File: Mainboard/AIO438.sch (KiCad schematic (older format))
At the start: 0 parts

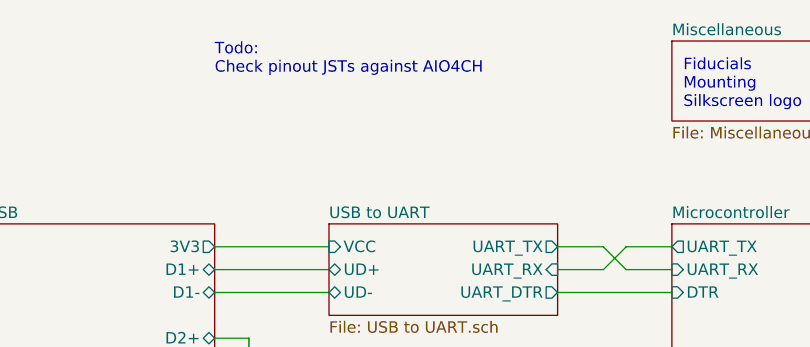
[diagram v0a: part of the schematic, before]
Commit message: Modify library references
As described in the README of the newly added libraries submodule.
Schematic and PCB are synced.

Hardware folder is renamed to mainboard
Any other PCBs can be put in their own subfolder in the gitrepo

Commit also swaps source/drain of Q1 because it appeared wrong for some
reason after updating all symbol/footprints.
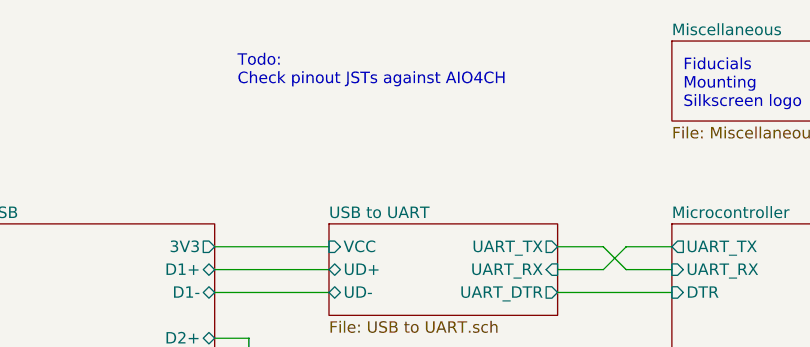
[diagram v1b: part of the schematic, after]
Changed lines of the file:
@@
 Wire Wire Line
 	6650 4200 6400 4200
-Text Notes 3350 1900 0    50   ~ 0
+Text Notes 3450 1950 0    50   ~ 0
 Todo:\nCheck pinout JSTs against AIO4CH
 Wire Wire Line

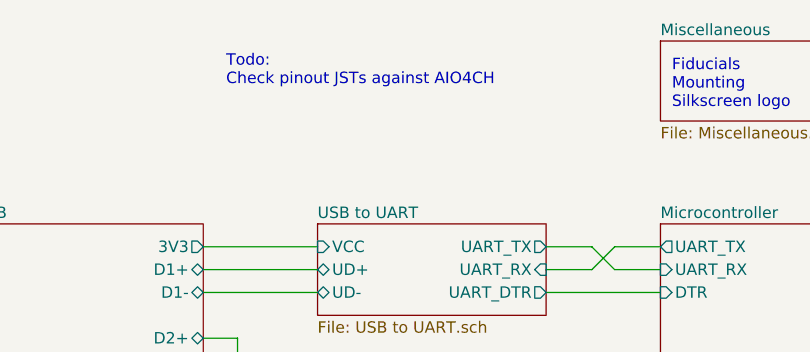
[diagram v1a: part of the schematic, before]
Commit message: Before power tree change
Backup before switching from two to one LDO
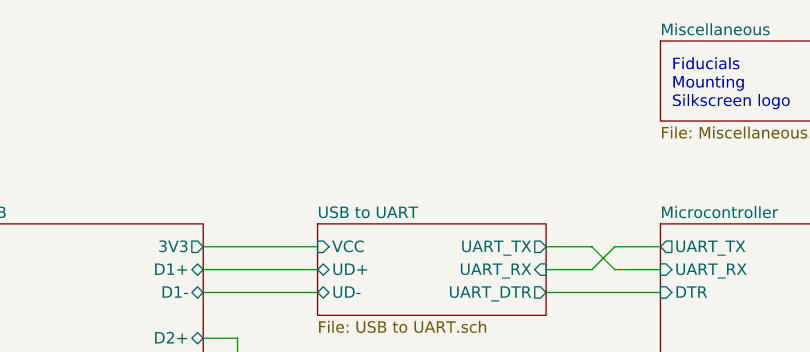
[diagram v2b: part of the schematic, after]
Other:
- note removed: "Todo:\nCheck pinout JSTs against AIO4CH"
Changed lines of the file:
@@
 Sheet 1 9
 Title "4x38W amp with DSP and BT"
-Date "2021-06-08"
-Rev "0.1"
+Date "2021-11-08"
+Rev "0.2"
 Comp "ZOUDIO"
 Comment1 ""
@@
 Wire Wire Line
 	6650 4200 6400 4200
-Text Notes 3450 1950 0    50   ~ 0
-Todo:\nCheck pinout JSTs against AIO4CH
 Wire Wire Line
 	3350 3150 3450 3150

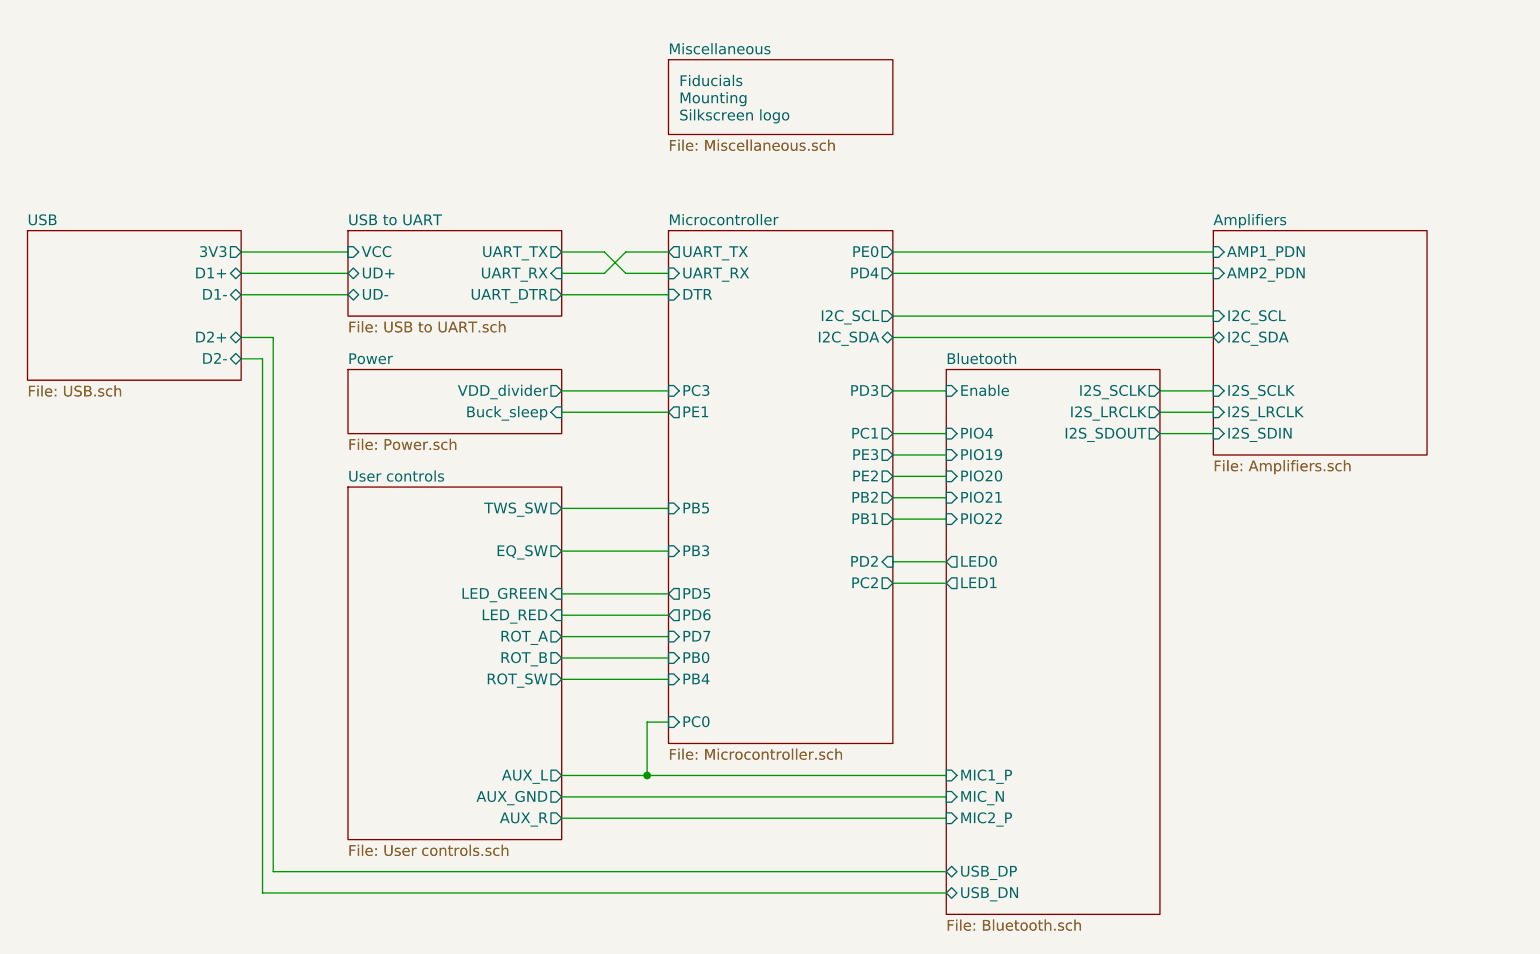
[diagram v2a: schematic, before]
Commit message: Before testing CH340B and VCHG
Cleaned up amp lay-out a bit in the meanwhile
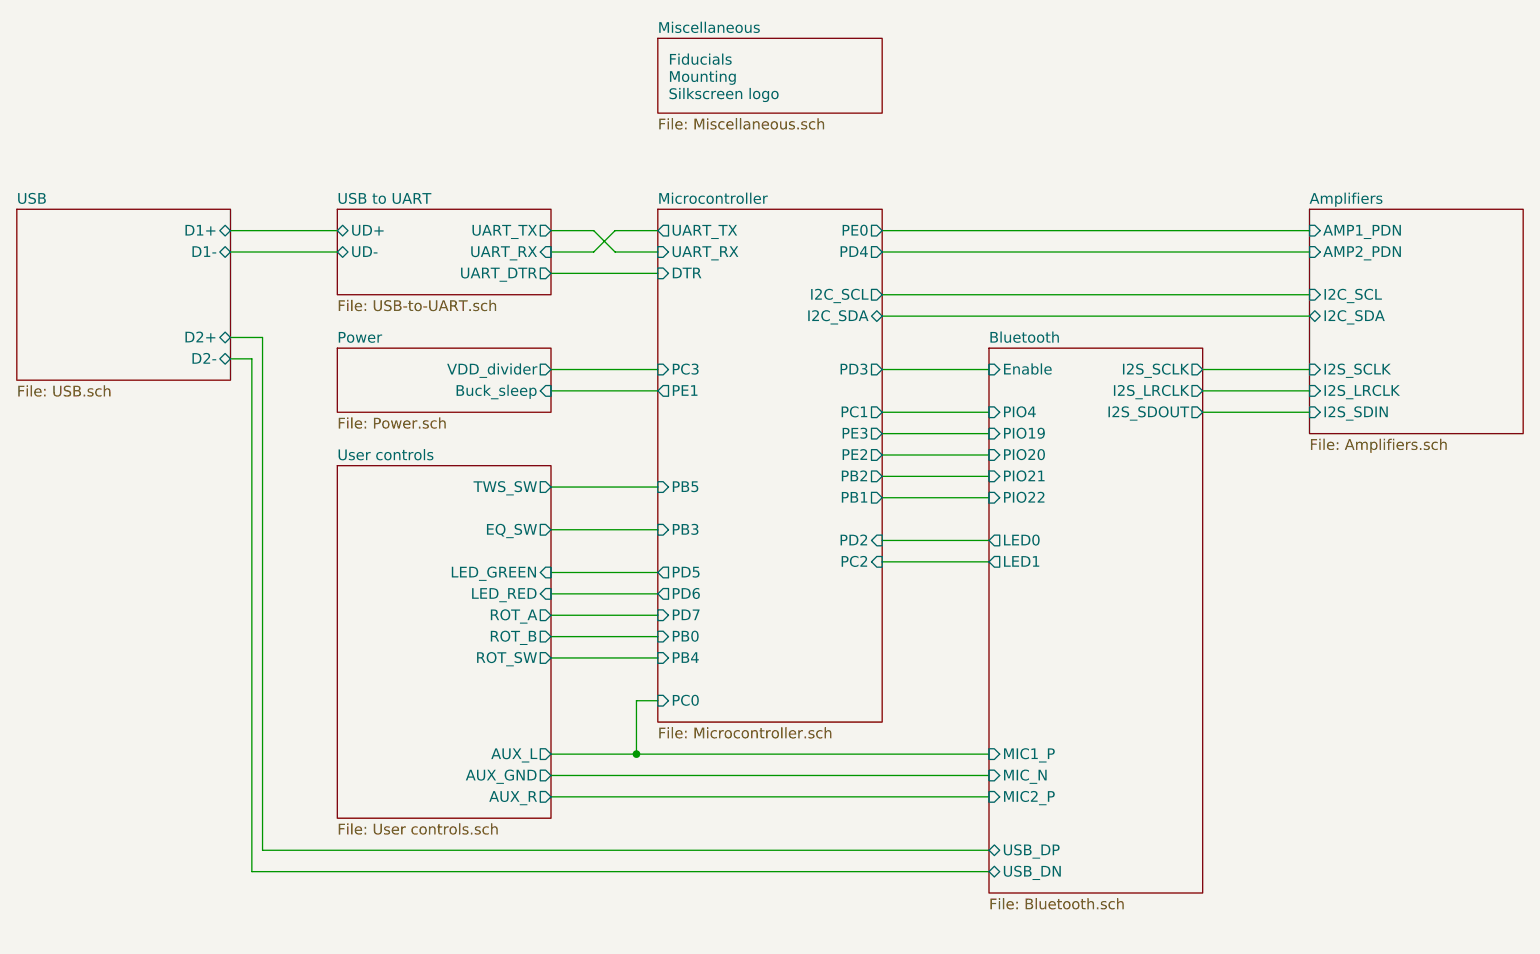
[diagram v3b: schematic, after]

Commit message: Result after weekend of lay-out
Pretty far, just neats to be cleaned up for production.
Does not pass DRC yet.
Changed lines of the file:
@@
 F3 "UART_RX" I R 4800 2650 50
 F4 "UART_DTR" O R 4800 2750 50
-F5 "UD+" B L 3800 2550 50
-F6 "UD-" B L 3800 2650 50
+F5 "D+" B L 3800 2550 50
+F6 "D-" B L 3800 2650 50
 $EndSheet
 Wire Wire Line

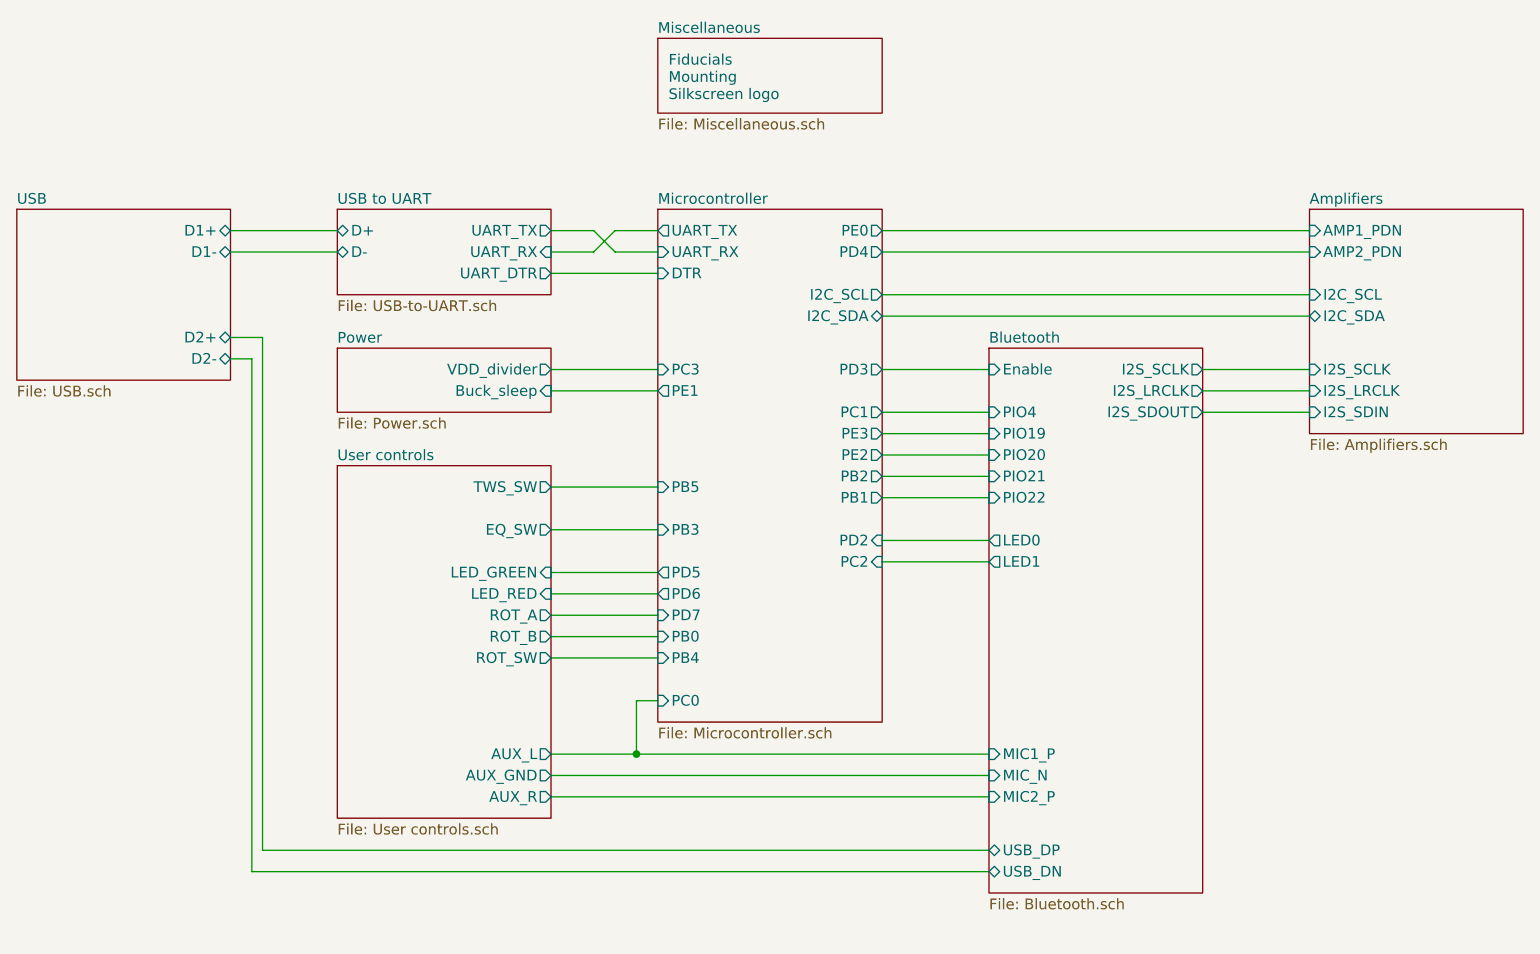
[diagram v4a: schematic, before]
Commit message: Mainboard: Version 1.0
Still need to clean up 3D models and BoM list,
but gerberexport-ready and ready to order.
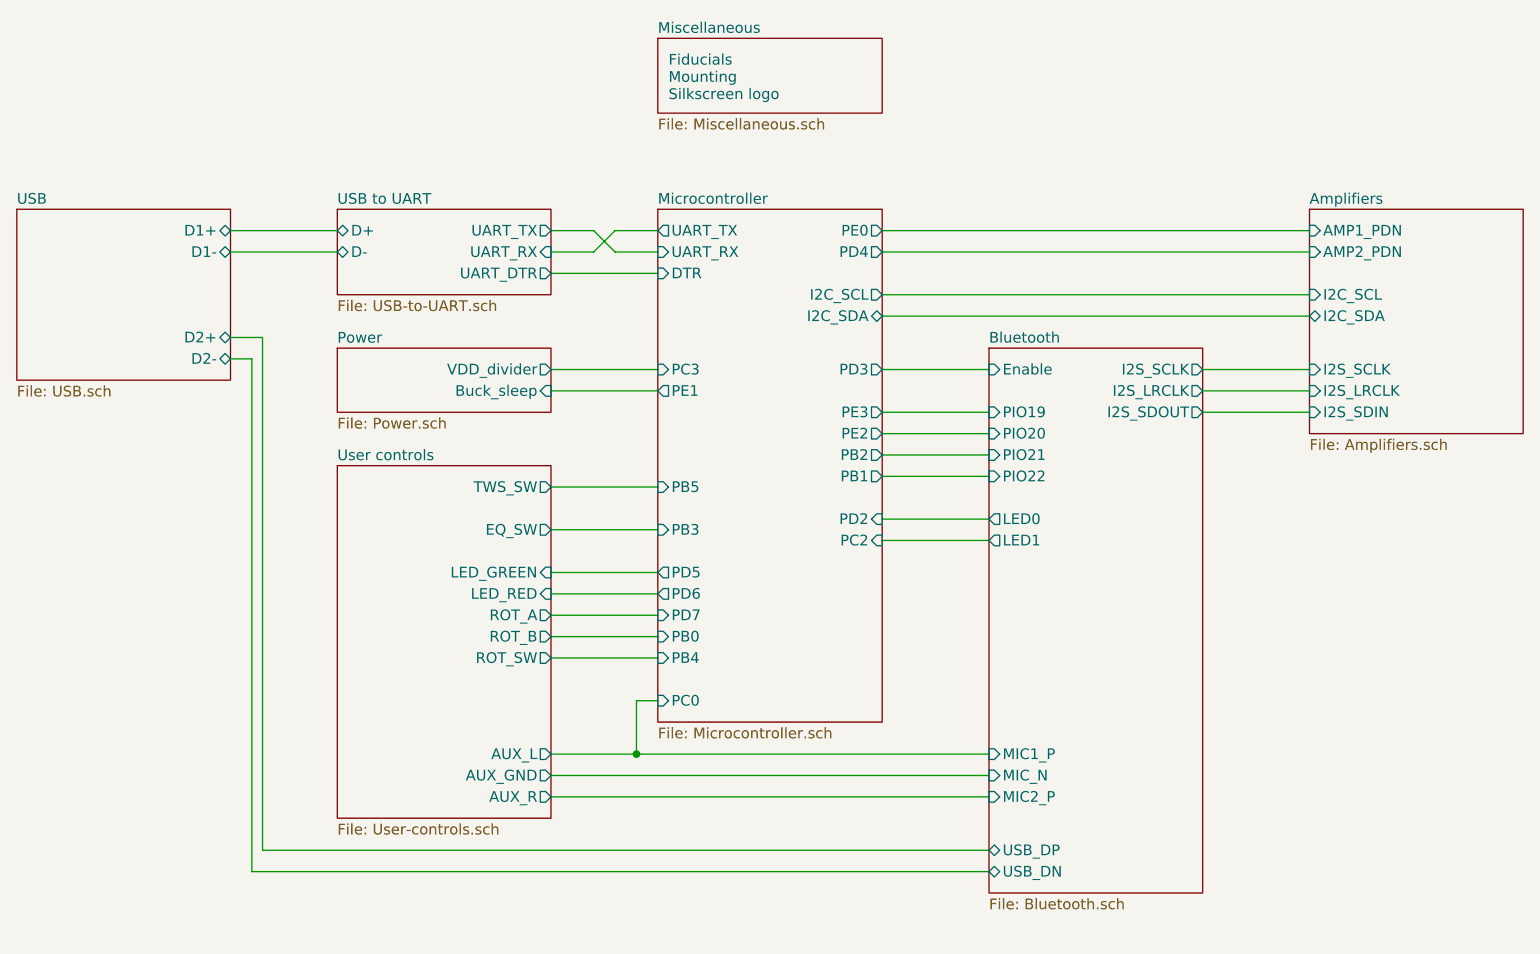
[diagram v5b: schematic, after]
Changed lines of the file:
@@
 Sheet 1 11
 Title "4x38W amp with DSP and BT"
-Date "2021-11-19"
-Rev "0.2"
+Date "2021-12-01"
+Rev "1.0"
 Comp "ZOUDIO"
 Comment1 ""
@@
 F3 "I2S_LRCLK" O R 7850 3300 50
 F4 "I2S_SCLK" O R 7850 3200 50
-F5 "PIO19" I L 6850 3500 50
-F6 "PIO22" I L 6850 3800 50
-F7 "PIO21" I L 6850 3700 50
-F8 "PIO20" I L 6850 3600 50
-F9 "LED1" O L 6850 4100 50
-F10 "LED0" O L 6850 4000 50
-F11 "PIO4" I L 6850 3400 50
-F12 "Enable" I L 6850 3200 50
-F13 "MIC1_P" I L 6850 5000 50
-F14 "MIC2_P" I L 6850 5200 50
-F15 "MIC_N" I L 6850 5100 50
-F16 "USB_DN" B L 6850 5550 50
-F17 "USB_DP" B L 6850 5450 50
+F5 "PIO19" I L 6850 3400 50
+F6 "PIO22" I L 6850 3700 50
+F7 "PIO21" I L 6850 3600 50
+F8 "PIO20" I L 6850 3500 50
+F9 "LED1" O L 6850 4000 50
+F10 "LED0" O L 6850 3900 50
+F11 "Enable" I L 6850 3200 50
+F12 "MIC1_P" I L 6850 5000 50
+F13 "MIC2_P" I L 6850 5200 50
+F14 "MIC_N" I L 6850 5100 50
+F15 "USB_DN" B L 6850 5550 50
+F16 "USB_DP" B L 6850 5450 50
 $EndSheet
 $Sheet
@@
 U 60BE11E8
 F0 "User controls" 50
-F1 "User controls.sch" 50
+F1 "User-controls.sch" 50
 F2 "AUX_L" O R 4800 5000 50
 F3 "AUX_GND" O R 4800 5100 50
@@
 Wire Wire Line
 	3450 5450 3450 3050
+Wire Wire Line
+	3400 5550 6850 5550
+Wire Wire Line
+	6350 3200 6850 3200
+Wire Wire Line
+	6350 3400 6850 3400
+Wire Wire Line
+	6350 3500 6850 3500
+Wire Wire Line
+	6350 3600 6850 3600
+Wire Wire Line
+	6350 3700 6850 3700
+Wire Wire Line
+	6350 3900 6850 3900
+Wire Wire Line
+	6350 4000 6850 4000
+Connection ~ 5200 5000
+Wire Wire Line
+	6350 2550 8350 2550
+Wire Wire Line
+	6350 2650 8350 2650
+Wire Wire Line
+	6350 2850 8350 2850
+Wire Wire Line
+	7850 3200 8350 3200
+Wire Wire Line
+	7850 3300 8350 3300
+Wire Wire Line
+	7850 3400 8350 3400
 $Sheet
 S 5300 2450 1050 2400
@@
 F0 "Microcontroller" 50
 F1 "Microcontroller.sch" 50
-F2 "PE3" O R 6350 3500 50
+F2 "PE3" O R 6350 3400 50
 F3 "I2C_SCL" O R 6350 2850 50
 F4 "PC3" I L 5300 3200 50
 F5 "PE1" O L 5300 3300 50
 F6 "I2C_SDA" B R 6350 2950 50
-F7 "PD2" I R 6350 4000 50
-F8 "PC1" O R 6350 3400 50
-F9 "PC0" I L 5300 4750 50
-F10 "PD4" O R 6350 2650 50
-F11 "PE0" O R 6350 2550 50
-F12 "PD6" O L 5300 4250 50
-F13 "PD5" O L 5300 4150 50
-F14 "UART_TX" O L 5300 2550 50
-F15 "UART_RX" I L 5300 2650 50
-F16 "PB0" I L 5300 4450 50
-F17 "PB1" O R 6350 3800 50
-F18 "PB2" O R 6350 3700 50
-F19 "PB3" I L 5300 3950 50
-F20 "PB4" I L 5300 4550 50
-F21 "DTR" I L 5300 2750 50
-F22 "PD7" I L 5300 4350 50
-F23 "PB5" I L 5300 3750 50
-F24 "PE2" O R 6350 3600 50
-F25 "PD3" O R 6350 3200 50
-F26 "PC2" I R 6350 4100 50
-$EndSheet
-Wire Wire Line
-	3400 5550 6850 5550
-Wire Wire Line
-	6350 3200 6850 3200
-Wire Wire Line
-	6350 3400 6850 3400
-Wire Wire Line
-	6350 3500 6850 3500
-Wire Wire Line
-	6350 3600 6850 3600
-Wire Wire Line
-	6350 3700 6850 3700
-Wire Wire Line
-	6350 3800 6850 3800
-Wire Wire Line
-	6350 4000 6850 4000
-Wire Wire Line
-	6350 4100 6850 4100
-Connection ~ 5200 5000
-Wire Wire Line
-	6350 2550 8350 2550
-Wire Wire Line
-	6350 2650 8350 2650
-Wire Wire Line
-	6350 2850 8350 2850
-Wire Wire Line
-	7850 3200 8350 3200
-Wire Wire Line
-	7850 3300 8350 3300
-Wire Wire Line
-	7850 3400 8350 3400
+F7 "PD2" I R 6350 3900 50
+F8 "PC0" I L 5300 4750 50
+F9 "PD4" O R 6350 2650 50
+F10 "PE0" O R 6350 2550 50
+F11 "PD6" O L 5300 4250 50
+F12 "PD5" O L 5300 4150 50
+F13 "UART_TX" O L 5300 2550 50
+F14 "UART_RX" I L 5300 2650 50
+F15 "PB0" I L 5300 4450 50
+F16 "PB1" O R 6350 3700 50
+F17 "PB2" O R 6350 3600 50
+F18 "PB3" I L 5300 3950 50
+F19 "PB4" I L 5300 4550 50
+F20 "DTR" I L 5300 2750 50
+F21 "PD7" I L 5300 4350 50
+F22 "PB5" I L 5300 3750 50
+F23 "PE2" O R 6350 3500 50
+F24 "PD3" O R 6350 3200 50
+F25 "PC2" I R 6350 4000 50
+$EndSheet
 $EndSCHEMATC
